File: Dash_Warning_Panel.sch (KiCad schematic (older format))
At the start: 39 parts, among them J1 Conn, U1 TLC6C5816, U2 TPS22810

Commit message: 2020 Initial Design
2020 Initial Design Submission:
Connector changed to 8 pin Molex 90 degree KK
Added Seven Segment Display
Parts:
- removed HS1: Heatsink_Pad, symbol Mechanical:Heatsink_Pad
- C1, C2, C3, C4, C5, C6, C7: Digikey P/N (none) -> 399-11133-1-ND
- C8: Digikey P/N (none) -> 399-1096-1-ND; P/N (none) -> C0603C104K4RACTU
- D2, D3, D4, D5, D6: footprint LEDs:LED_Cree-PLCC4_2x2mm_CW -> OSRAM:OSRAM_PLCC-4_THERM_PAD
- J1: footprint Connectors_TE-Connectivity:TE_84953-6_1x06_P1.0mm_Horizontal -> Molex:Molex_KK-171857_08x2.54mm_Right_Angle; Digikey P/N A101400CT-ND -> WM10303-ND; MFG TE -> Molex; P/N ‎84953-6 -> 1718571008
- R1: value 11.3 -> 11; footprint Resistors_SMD:R_0603 -> Resistors_SMD:R_1210; Digikey P/N 541-27.4HCT-ND -> 541-11.0AACT-ND; P/N CRCW060327R4FKEA -> CRCW121011R0FKEA
- R10: value 86.6 -> 118; Digikey P/N (none) -> 541-118HCT-ND; MFG (none) -> Vishay; P/N ‎1-2176091-8 -> CRCW0603118RFKEA
- R11, R12, R13, R14, R15, R16, R17, R7, R8, R9: value 116.7 -> 118; Digikey P/N 541-27.4HCT-ND -> 541-118HCT-ND; P/N CRCW060327R4FKEA -> CRCW0603118RFKEA
- R2, R3, R4, R5, R6: value 71 -> 69.8; footprint Resistors_SMD:R_0603 -> Resistors_SMD:R_1206; Digikey P/N 541-27.4HCT-ND -> 541-69.8FCT-ND; P/N CRCW060327R4FKEA -> CRCW120669R8FKEA
- U1: Digikey P/N (none) -> 296-51674-1-ND; MFG (none) -> TI; P/N (none) -> TLC6C5816QPWPRQ1
- U2: Digikey P/N (none) -> 296-45297-1-ND
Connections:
- net labels removed: HS
- wire segments 151 -> 152
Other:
- note added: "*Pad 26 Net reused as heatsink \npad net for flood fill clearancing"
- note added: "Blue: LCB G6SP\nIfm = 250mA, Ifn = 150mA\nVf = 3.3V, Vin = 5.0V\nVr = 5-3.3= 1.70V\nR = 1.70V/150mA = 11.3 Ohm\nVrm = 2.1V, Irm = 200mA\nVrmin = 10.5 Ohm\nPr = 2.1 * 200mA = 0.42W"
- note added: "Green: KP DELPS\nIfm = 20mA, Ifn = 18mA\nVf = 2.9V, Vin = 5.0V\nVr = 5-2.9= 2.10V\nR = 2.10V/18mA = 116.7 Ohm\nVrm = 2.3V, Irm = 20mA\nVrmin = 115 Ohm\nPr = 2.3 * 20mA = 0.046W"
- note added: "Red: LS E6SF\nIfm = 70mA, Ifn = 40mA\nVf = 2.15V, Vin = 5.0V\nVr = 5.0-2.15 = 2.85V\nR = 2.85V/40mA = 71.25 Ohm\nVrm = 3.0V, Irm = 50mA\nVrmin = 60 Ohm\nPr = 3V * 50mA = 0.15W"
- note added: "Seg: DSM7TA56105T\nIfm = 20mA, Ifn = 18mA\nVf = 3.0V, Vin = 5.0V\nVr = 5-3.0= 2.00V\nR = 2.00V/18mA = 111.1 Ohm\nVrm = 2.2V, Irm = 20mA\nVrmin = 110 Ohm\nPr = 2.2V * 20mA = 0.044W"
- note added: "Yellow: LY E6SF\nIfm = 70mA, Ifn = 40mA\nVf = 2.15V, Vin = 5.0V\nVr = 5.0-2.15 = 2.85V\nR = 2.85V/40mA = 71.25 Ohm\nVrm = 3.0V, Irm = 50mA\nVrmin = 60 Ohm\nPr = 3V * 50mA = 0.15W"
- note removed: "Blue: LCB G6SP\nIfm = 250mA, Ifn = 150mA\nVf = 3.3V, Vin = 5.0V\nVr = 5-3.3= 1.70V\nR = 1.70V/150mA = 11.3 Ohm\nVrm = 2.1V, Irm = 200mA\nVrmin = 10.5 Ohm"
- note removed: "Green: KP DELPS\nIfm = 20mA, Ifn = 18mA\nVf = 2.9V, Vin = 5.0V\nVr = 5-2.9= 2.10V\nR = 2.10V/18mA = 116.7 Ohm\nVrm = 2.3V, Irm = 20mA\nVrmin = 115 Ohm"
- note removed: "Red: LS E6SF\nIfm = 70mA, Ifn = 40mA\nVf = 2.15V, Vin = 5.0V\nVr = 5.0-2.15 = 2.85V\nR = 2.85V/40mA = 71.25 Ohm\nVrm = 3.0V, Irm = 50mA\nVrmin = 60 Ohm"
- note removed: "Seg: DSM7TA56105T\nIfm = 20mA, Ifn = 18mA\nVf = 3.0V, Vin = 5.0V\nVr = 5-3.0= 2.00V\nR = 2.00V/18mA = 111.1 Ohm\nVrm = 2.2V, Irm = 20mA\nVrmin = 110 Ohm"
- note removed: "Yellow: LY E6SF\nIfm = 70mA, Ifn = 40mA\nVf = 2.15V, Vin = 5.0V\nVr = 5.0-2.15 = 2.85V\nR = 2.85V/40mA = 71.25 Ohm\nVrm = 3.0V, Irm = 50mA\nVrmin = 60 Ohm"

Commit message: First Manufacture Ready 2020
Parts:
- C1, C2, C3, C4, C5, C6, C7: Digikey P/N 399-11133-1-ND -> (none); MFG KEMET -> (none); P/N C0603C105K8RACTU -> (none)
- C8: Description (none) -> CAP CER 0.1UF 16V X7R 0603; Digikey P/N 399-1096-1-ND -> (none); P/N C0603C104K4RACTU -> C0603C104M4RACTU
- D2, D6: value LY E6SF -> SM1206NYC-IL; footprint OSRAM:OSRAM_PLCC-4_THERM_PAD -> LEDs:LED_1206; Description (none) -> LED YELLOW CLEAR 1206 SMD; Digikey P/N 475-3790-1-ND -> (none); MFG OSRAM -> BIVAR; P/N LY E6SF-ABCA-36-3B5A-50-R18-Z -> SM1206NYC-IL
- D3, D4, D5: value LS E6SF -> SM1206NHC-IL; footprint OSRAM:OSRAM_PLCC-4_THERM_PAD -> LEDs:LED_1206; Description (none) -> LED RED CLEAR 1206 SMD; Digikey P/N 475-3432-1-ND -> (none); MFG OSRAM -> BIVAR; P/N LS E67F-ABBB-1-1-Z -> SM1206NHC-IL
- D7, D8, D9: value KP DELPS -> SM1206NPGC-IL; footprint OSRAM:PLCC-2 -> LEDs:LED_1206; Description (none) -> LED GREEN CLEAR 1206 SMD; Digikey P/N 475-3715-1-ND -> (none); MFG OSRAM -> BIVAR; P/N KP DELPS1.FP-UGVI-34-Z555-10-S -> SM1206NPGC-IL
- J1: footprint Molex:Molex_KK-171857_08x2.54mm_Right_Angle -> FSAE-Dash-Warning-Panel:8wireConn; Digikey P/N WM10303-ND -> N/A; MFG Molex -> N/A; P/N 1718571008 -> N/A
- R1: Digikey P/N 541-11.0AACT-ND -> (none)
- R10, R11, R12, R13, R14, R15, R16, R17, R7, R8, R9: value 118 -> 120; Description (none) -> RES 120 OHM 1% 1/10W 0603; Digikey P/N 541-118HCT-ND -> RMCF0603FT120RCT-ND; MFG Vishay -> Stackpole; P/N CRCW0603118RFKEA -> RMCF0603FT120R
- R2, R3, R4, R5, R6: value 69.8 -> 120; footprint Resistors_SMD:R_1206 -> Resistors_SMD:R_0603; Description (none) -> RES 120 OHM 1% 1/10W 0603; Digikey P/N 541-69.8FCT-ND -> RMCF0603FT120RCT-ND; MFG Vishay -> Stackpole; P/N CRCW120669R8FKEA -> RMCF0603FT120R
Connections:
- net GND: now also U1.29 (HS)
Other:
- note added: "Green - SM1206NPGC-IL\nVf = 3V, 1550mcd @ 523nm\nIf = 20mA, Ifp = 100mA\nMin R: 100 Ohm\nPr = 2.0 * 20mA = 0.040W"
- note added: "Red SM1206NHC-IL\nVf = 2.1V, 1250mcd @ 630nm\nIf = 25mA, Ifp = 100mA\nVin = 5.0V\nVr = 5.0-2.10 = 2.90V\nR = 2.90V/25mA = 116 Ohm\nPr = 2.9V * 25mA = 0.0725W"
- note added: "Yellow - SM1206NYC-IL\nVf = 2.0V, 1000mcd @ 590nm\nIf = 25mA, Ifp = 100mA\nMin R: 120 Ohm\nPr = 3V * 25mA = 0.075W"
- note removed: "*Pad 26 Net reused as heatsink \npad net for flood fill clearancing"
- note removed: "Green: KP DELPS\nIfm = 20mA, Ifn = 18mA\nVf = 2.9V, Vin = 5.0V\nVr = 5-2.9= 2.10V\nR = 2.10V/18mA = 116.7 Ohm\nVrm = 2.3V, Irm = 20mA\nVrmin = 115 Ohm\nPr = 2.3 * 20mA = 0.046W"
- note removed: "Red: LS E6SF\nIfm = 70mA, Ifn = 40mA\nVf = 2.15V, Vin = 5.0V\nVr = 5.0-2.15 = 2.85V\nR = 2.85V/40mA = 71.25 Ohm\nVrm = 3.0V, Irm = 50mA\nVrmin = 60 Ohm\nPr = 3V * 50mA = 0.15W"
- note removed: "Yellow: LY E6SF\nIfm = 70mA, Ifn = 40mA\nVf = 2.15V, Vin = 5.0V\nVr = 5.0-2.15 = 2.85V\nR = 2.85V/40mA = 71.25 Ohm\nVrm = 3.0V, Irm = 50mA\nVrmin = 60 Ohm\nPr = 3V * 50mA = 0.15W"

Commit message: Updated BOM and part number data
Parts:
- C1, C2, C3, C4, C5, C6, C7: Description (none) -> CAP CER 1.0UF 16V X7R 0603; Digikey P/N (none) -> 399-7847-1-ND; MFG (none) -> KEMET; P/N (none) -> C0603C105K4RACTU
- C8: Digikey P/N (none) -> 399-1099-1-ND
- D1: Description (none) -> LED BLUE, 3.3V 140mA
- D10: Description (none) -> DISPLAY 7SEG 0.56\" SGL GRN 10SMD
- D2, D6: Digikey P/N (none) -> 492-1947-1-ND
- D3, D4, D5: Digikey P/N (none) -> 492-1944-1-ND
- D7, D8, D9: Digikey P/N (none) -> 492-1945-1-ND
- J1: Description (none) -> Wire Solder Points
- R1: Description (none) -> RES SMD 11 OHM 1% 1/2W 1210; Digikey P/N (none) -> 541-11.0AACT-ND
- U1: Description (none) -> LED Driver IC 16 Output Linear Shift Register PWM Dimming
- U2: Description (none) -> IC PWR SWITCH N-CHAN 1:1 SOT23-6
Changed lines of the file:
@@
 F 2 "Capacitors_SMD:C_0603" H 5038 1000 50  0001 C CNN
 F 3 "" H 5000 1150 50  0001 C CNN
-F 4 "" H 0   0   50  0001 C CNN "P/N"
-F 5 "" H 5000 1150 50  0001 C CNN "MFG"
-F 6 "" H 5000 1150 50  0001 C CNN "Digikey P/N"
+F 4 "C0603C105K4RACTU" H 0   0   50  0001 C CNN "P/N"
+F 5 "KEMET" H 5000 1150 50  0001 C CNN "MFG"
+F 6 "399-7847-1-ND" H 5000 1150 50  0001 C CNN "Digikey P/N"
+F 7 "CAP CER 1.0UF 16V X7R 0603" H 5000 1150 50  0001 C CNN "Description"
 	1    5000 1150
 	1    0    0    -1
@@
 F 2 "Capacitors_SMD:C_0603" H 5338 1000 50  0001 C CNN
 F 3 "" H 5300 1150 50  0001 C CNN
-F 4 "" H 0   0   50  0001 C CNN "P/N"
-F 5 "" H 5300 1150 50  0001 C CNN "MFG"
-F 6 "" H 5300 1150 50  0001 C CNN "Digikey P/N"
+F 4 "C0603C105K4RACTU" H 0   0   50  0001 C CNN "P/N"
+F 5 "KEMET" H 5300 1150 50  0001 C CNN "MFG"
+F 6 "399-7847-1-ND" H 5300 1150 50  0001 C CNN "Digikey P/N"
+F 7 "CAP CER 1.0UF 16V X7R 0603" H 5300 1150 50  0001 C CNN "Description"
 	1    5300 1150
 	1    0    0    -1
@@
 F 2 "Capacitors_SMD:C_0603" H 5638 1000 50  0001 C CNN
 F 3 "" H 5600 1150 50  0001 C CNN
-F 4 "" H 0   0   50  0001 C CNN "P/N"
-F 5 "" H 5600 1150 50  0001 C CNN "MFG"
-F 6 "" H 5600 1150 50  0001 C CNN "Digikey P/N"
+F 4 "C0603C105K4RACTU" H 0   0   50  0001 C CNN "P/N"
+F 5 "KEMET" H 5600 1150 50  0001 C CNN "MFG"
+F 6 "399-7847-1-ND" H 5600 1150 50  0001 C CNN "Digikey P/N"
+F 7 "CAP CER 1.0UF 16V X7R 0603" H 5600 1150 50  0001 C CNN "Description"
 	1    5600 1150
 	1    0    0    -1
@@
 F 5 "N/A" H 1950 3600 50  0001 C CNN "Digikey P/N"
 F 6 "N/A" H 1950 3600 50  0001 C CNN "MFG"
+F 7 "Wire Solder Points" H 1950 3600 50  0001 C CNN "Description"
 	1    1950 3600
 	-1   0    0    -1
@@
 F 3 "https://www.bivar.com/Files/Datasheets/SM1206NYC-IL.pdf" H 7650 4600 50  0001 C CNN
 F 4 "SM1206NYC-IL" H 300 -1000 50  0001 C CNN "P/N"
-F 5 "" H 7650 4600 50  0001 C CNN "Digikey P/N"
+F 5 "492-1947-1-ND" H 7650 4600 50  0001 C CNN "Digikey P/N"
 F 6 "BIVAR" H 7650 4600 50  0001 C CNN "MFG"
 F 7 "LED YELLOW CLEAR 1206 SMD" H 7650 4600 50  0001 C CNN "Description"
@@
 F 5 "TI" H 3550 1150 50  0001 C CNN "MFG"
 F 6 "296-45297-1-ND" H 3550 1150 50  0001 C CNN "Digikey P/N"
+F 7 "IC PWR SWITCH N-CHAN 1:1 SOT23-6" H 3550 1150 50  0001 C CNN "Description"
 	1    3550 1150
 	1    0    0    -1
@@
 F 2 "Capacitors_SMD:C_0603" H 2838 1450 50  0001 C CNN
 F 3 "" H 2800 1600 50  0001 C CNN
-F 4 "" H 0   0   50  0001 C CNN "P/N"
-F 5 "" H 2800 1600 50  0001 C CNN "MFG"
-F 6 "" H 2800 1600 50  0001 C CNN "Digikey P/N"
+F 4 "C0603C105K4RACTU" H 0   0   50  0001 C CNN "P/N"
+F 5 "KEMET" H 2800 1600 50  0001 C CNN "MFG"
+F 6 "399-7847-1-ND" H 2800 1600 50  0001 C CNN "Digikey P/N"
+F 7 "CAP CER 1.0UF 16V X7R 0603" H 2800 1600 50  0001 C CNN "Description"
 	1    2800 1600
 	-1   0    0    1
@@
 F 2 "Capacitors_SMD:C_0603" H 4388 1450 50  0001 C CNN
 F 3 "" H 4350 1600 50  0001 C CNN
-F 4 "" H 0   0   50  0001 C CNN "P/N"
-F 5 "" H 4350 1600 50  0001 C CNN "MFG"
-F 6 "" H 4350 1600 50  0001 C CNN "Digikey P/N"
+F 4 "C0603C105K4RACTU" H 0   0   50  0001 C CNN "P/N"
+F 5 "KEMET" H 4350 1600 50  0001 C CNN "MFG"
+F 6 "399-7847-1-ND" H 4350 1600 50  0001 C CNN "Digikey P/N"
+F 7 "CAP CER 1.0UF 16V X7R 0603" H 4350 1600 50  0001 C CNN "Description"
 	1    4350 1600
 	-1   0    0    1
@@
 F 2 "Capacitors_SMD:C_0603" H 2588 3050 50  0001 C CNN
 F 3 "" H 2550 3200 50  0001 C CNN
-F 4 "" H 0   0   50  0001 C CNN "P/N"
-F 5 "" H 2550 3200 50  0001 C CNN "MFG"
-F 6 "" H 2550 3200 50  0001 C CNN "Digikey P/N"
+F 4 "C0603C105K4RACTU" H 0   0   50  0001 C CNN "P/N"
+F 5 "KEMET" H 2550 3200 50  0001 C CNN "MFG"
+F 6 "399-7847-1-ND" H 2550 3200 50  0001 C CNN "Digikey P/N"
+F 7 "CAP CER 1.0UF 16V X7R 0603" H 2550 3200 50  0001 C CNN "Description"
 	1    2550 3200
 	1    0    0    -1
@@
 F 1 "LCB G6SP" H 6450 1450 50  0000 C CNN
 F 2 "OSRAM:PLCC-6_THERM_MOD" H 6450 1350 50  0001 C CNN
-F 3 "" H 6450 1350 50  0001 C CNN
+F 3 "https://dammedia.osram.info/media/resource/hires/osram-dam-6030625/LCB%20G6SP_EN.pdf" H 6450 1350 50  0001 C CNN
 F 4 "LCB G6SP-DBFA-4J5L-0-140-R18-Z" H -900 -4250 50  0001 C CNN "P/N"
 F 5 "475-3674-1-ND" H 6450 1350 50  0001 C CNN "Digikey P/N"
 F 6 "OSRAM" H 6450 1350 50  0001 C CNN "MFG"
+F 7 "LED BLUE, 3.3V 140mA" H 6450 1350 50  0001 C CNN "Description"
 	1    6450 1350
 	0    -1   -1   0
@@
 F 3 "https://www.bivar.com/Portals/0/Products/SM1206NHC-IL.pdf" H 7650 4250 50  0001 C CNN
 F 4 "SM1206NHC-IL" H 300 -1350 50  0001 C CNN "P/N"
-F 5 "" H 7650 4250 50  0001 C CNN "Digikey P/N"
+F 5 "492-1944-1-ND" H 7650 4250 50  0001 C CNN "Digikey P/N"
 F 6 "BIVAR" H 7650 4250 50  0001 C CNN "MFG"
 F 7 "LED RED CLEAR 1206 SMD" H 7650 4250 50  0001 C CNN "Description"
@@
 F 1 "11" V 6450 1750 50  0000 C CNN
 F 2 "Resistors_SMD:R_1210" V 6380 1750 50  0001 C CNN
-F 3 "" H 6450 1750 50  0001 C CNN
+F 3 "http://www.vishay.com/docs/20035/dcrcwe3.pdf" H 6450 1750 50  0001 C CNN
 F 4 "CRCW121011R0FKEA" H -450 -3850 50  0001 C CNN "P/N"
-F 5 "" H 6450 1750 50  0001 C CNN "Digikey P/N"
+F 5 "541-11.0AACT-ND" H 6450 1750 50  0001 C CNN "Digikey P/N"
 F 6 "Vishay" H 6450 1750 50  0001 C CNN "MFG"
+F 7 "RES SMD 11 OHM 1% 1/2W 1210" H 6450 1750 50  0001 C CNN "Description"
 	1    6450 1750
 	1    0    0    -1
@@
 F 3 "https://www.bivar.com/Portals/0/Products/SM1206NHC-IL.pdf" H 7650 3900 50  0001 C CNN
 F 4 "SM1206NHC-IL" H 300 -1700 50  0001 C CNN "P/N"
-F 5 "" H 7650 3900 50  0001 C CNN "Digikey P/N"
+F 5 "492-1944-1-ND" H 7650 3900 50  0001 C CNN "Digikey P/N"
 F 6 "BIVAR" H 7650 3900 50  0001 C CNN "MFG"
 F 7 "LED RED CLEAR 1206 SMD" H 7650 3900 50  0001 C CNN "Description"
@@
 F 3 "https://www.bivar.com/Portals/0/Products/SM1206NHC-IL.pdf" H 7650 3550 50  0001 C CNN
 F 4 "SM1206NHC-IL" H 300 -2050 50  0001 C CNN "P/N"
-F 5 "" H 7650 3550 50  0001 C CNN "Digikey P/N"
+F 5 "492-1944-1-ND" H 7650 3550 50  0001 C CNN "Digikey P/N"
 F 6 "BIVAR" H 7650 3550 50  0001 C CNN "MFG"
 F 7 "LED RED CLEAR 1206 SMD" H 7650 3550 50  0001 C CNN "Description"
@@
 F 3 "https://www.bivar.com/Files/Datasheets/SM1206NYC-IL.pdf" H 7650 3200 50  0001 C CNN
 F 4 "SM1206NYC-IL" H 300 -2400 50  0001 C CNN "P/N"
-F 5 "" H 7650 3200 50  0001 C CNN "Digikey P/N"
+F 5 "492-1947-1-ND" H 7650 3200 50  0001 C CNN "Digikey P/N"
 F 6 "BIVAR" H 7650 3200 50  0001 C CNN "MFG"
 F 7 "LED YELLOW CLEAR 1206 SMD" H 7650 3200 50  0001 C CNN "Description"
@@
 F 3 "https://www.bivar.com/parts_content/Datasheets/SM1206NPGC-IL.pdf" H 7650 2850 50  0001 C CNN
 F 4 "SM1206NPGC-IL" H 300 -2750 50  0001 C CNN "P/N"
-F 5 "" H 7650 2850 50  0001 C CNN "Digikey P/N"
+F 5 "492-1945-1-ND" H 7650 2850 50  0001 C CNN "Digikey P/N"
 F 6 "BIVAR" H 7650 2850 50  0001 C CNN "MFG"
 F 7 "LED GREEN CLEAR 1206 SMD" H 7650 2850 50  0001 C CNN "Description"
@@
 F 3 "https://www.bivar.com/parts_content/Datasheets/SM1206NPGC-IL.pdf" H 7650 2500 50  0001 C CNN
 F 4 "SM1206NPGC-IL" H 300 -3100 50  0001 C CNN "P/N"
-F 5 "" H 7650 2500 50  0001 C CNN "Digikey P/N"
+F 5 "492-1945-1-ND" H 7650 2500 50  0001 C CNN "Digikey P/N"
 F 6 "BIVAR" H 7650 2500 50  0001 C CNN "MFG"
 F 7 "LED GREEN CLEAR 1206 SMD" H 7650 2500 50  0001 C CNN "Description"
@@
 F 3 "https://www.bivar.com/parts_content/Datasheets/SM1206NPGC-IL.pdf" H 7650 2150 50  0001 C CNN
 F 4 "SM1206NPGC-IL" H 300 -3450 50  0001 C CNN "P/N"
-F 5 "" H 7650 2150 50  0001 C CNN "Digikey P/N"
+F 5 "492-1945-1-ND" H 7650 2150 50  0001 C CNN "Digikey P/N"
 F 6 "BIVAR" H 7650 2150 50  0001 C CNN "MFG"
 F 7 "LED GREEN CLEAR 1206 SMD" H 7650 2150 50  0001 C CNN "Description"
@@
 F 5 "DSM7TA56105TCT-ND" H 7050 5850 50  0001 C CNN "Digikey P/N"
 F 6 "DSM7TA56105T" H 7050 5850 50  0001 C CNN "P/N"
+F 7 "DISPLAY 7SEG 0.56\" SGL GRN 10SMD" H 7050 5850 50  0001 C CNN "Description"
 	1    7050 5850
 	1    0    0    -1
@@
 F 5 "TI" H 5550 3350 50  0001 C CNN "MFG"
 F 6 "TLC6C5816QPWPRQ1" H 5550 3350 50  0001 C CNN "P/N"
+F 7 "LED Driver IC 16 Output Linear Shift Register PWM Dimming" H 5550 3350 50  0001 C CNN "Description"
 	1    5550 3350
 	1    0    0    -1
@@
 F 2 "Capacitors_SMD:C_0603" H 4138 2650 50  0001 C CNN
 F 3 "" H 4100 2800 50  0001 C CNN
-F 4 "" H 1550 -400 50  0001 C CNN "P/N"
-F 5 "" H 4100 2800 50  0001 C CNN "MFG"
-F 6 "" H 4100 2800 50  0001 C CNN "Digikey P/N"
+F 4 "C0603C105K4RACTU" H 1550 -400 50  0001 C CNN "P/N"
+F 5 "KEMET" H 4100 2800 50  0001 C CNN "MFG"
+F 6 "399-7847-1-ND" H 4100 2800 50  0001 C CNN "Digikey P/N"
+F 7 "CAP CER 1.0UF 16V X7R 0603" H 4100 2800 50  0001 C CNN "Description"
 	1    4100 2800
 	1    0    0    -1
@@
 F 4 "C0603C104M4RACTU" H 1850 -400 50  0001 C CNN "P/N"
 F 5 "KEMET" H 4400 2800 50  0001 C CNN "MFG"
-F 6 "" H 4400 2800 50  0001 C CNN "Digikey P/N"
+F 6 "399-1099-1-ND" H 4400 2800 50  0001 C CNN "Digikey P/N"
 F 7 "CAP CER 0.1UF 16V X7R 0603" H 4400 2800 50  0001 C CNN "Description"
 	1    4400 2800
@@
 	2950 3400 2550 3400
 Connection ~ 2550 3400
+$Comp
+L power:GND #PWR?
+U 1 1 5EF8AEF3
+P 5450 4250
+F 0 "#PWR?" H 5450 4000 50  0001 C CNN
+F 1 "GND" H 5455 4077 50  0000 C CNN
+F 2 "" H 5450 4250 50  0001 C CNN
+F 3 "" H 5450 4250 50  0001 C CNN
+	1    5450 4250
+	1    0    0    -1
+$EndComp
 Wire Bus Line
 	4700 4850 6750 4850
@@
 Wire Bus Line
 	4700 3050 4700 4850
-$Comp
-L power:GND #PWR?
-U 1 1 5EF8AEF3
-P 5450 4250
-F 0 "#PWR?" H 5450 4000 50  0001 C CNN
-F 1 "GND" H 5455 4077 50  0000 C CNN
-F 2 "" H 5450 4250 50  0001 C CNN
-F 3 "" H 5450 4250 50  0001 C CNN
-	1    5450 4250
-	1    0    0    -1
-$EndComp
 $EndSCHEMATC

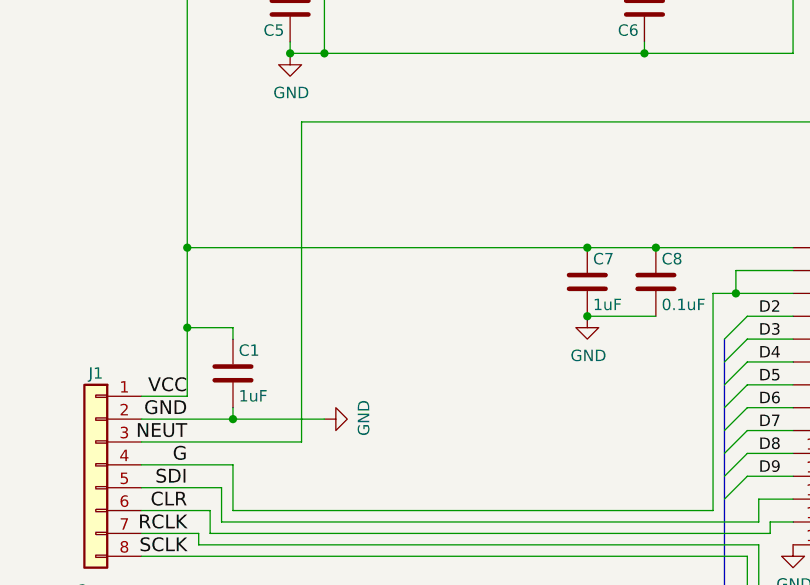
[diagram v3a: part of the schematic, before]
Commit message: Added LDO 3.3V Reg
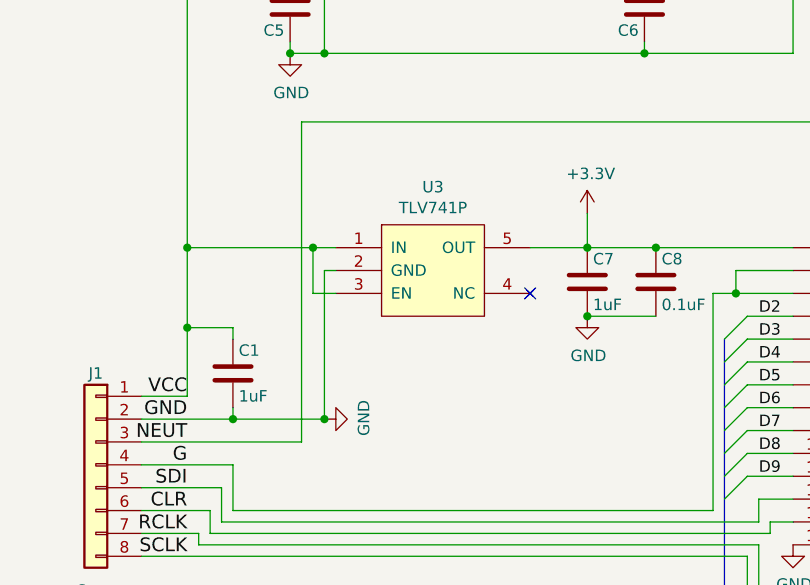
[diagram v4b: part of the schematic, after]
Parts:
- added U3: TLV741P, TO_SOT_Packages_SMD:SOT-23-5, symbol TI-addition:TLV741P
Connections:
- net GND: now also U3.2 (GND)
- net VCC: now also U3.1 (IN), U3.3 (EN); no longer C7.1, C8.1, U1.1 (VCC)
- new net +3V3: C7.1, C8.1, U1.1 (VCC), U3.5 (OUT)
- no-connect marks 5 -> 6
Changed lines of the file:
@@
 Wire Wire Line
 	2350 3300 2150 3300
-Wire Wire Line
-	2350 1000 2350 2650
 $Comp
 L Device:LED_ALT D2
@@
 Wire Wire Line
 	2150 4000 4800 4000
-Wire Wire Line
-	4100 2650 2350 2650
-Connection ~ 4100 2650
-Connection ~ 2350 2650
-Wire Wire Line
-	2350 2650 2350 3000
 Text Label 2350 3800 2    60   ~ 0
 CLR
@@
 Connection ~ 2550 3400
 $Comp
-L power:GND #PWR?
+L power:GND #PWR0106
 U 1 1 5EF8AEF3
 P 5450 4250
-F 0 "#PWR?" H 5450 4000 50  0001 C CNN
+F 0 "#PWR0106" H 5450 4000 50  0001 C CNN
 F 1 "GND" H 5455 4077 50  0000 C CNN
 F 2 "" H 5450 4250 50  0001 C CNN
@@
 	1    0    0    -1
 $EndComp
+Wire Wire Line
+	2350 1000 2350 2650
+$Comp
+L TI-addition:TLV741P U3
+U 1 1 5F3CBD45
+P 3400 2750
+F 0 "U3" H 3425 3115 50  0000 C CNN
+F 1 "TLV741P" H 3425 3024 50  0000 C CNN
+F 2 "TO_SOT_Packages_SMD:SOT-23-5" H 3400 2400 50  0001 C CNN
+F 3 "https://www.ti.com/lit/ds/symlink/tlv741p.pdf" H 3000 2850 50  0001 C CNN
+F 4 "IC REG LINEAR 3.3V 150MA SOT23-5" H 3400 2750 50  0001 C CNN "Description"
+F 5 "296-48987-1-ND" H 3400 2750 50  0001 C CNN "Digikey P/N"
+F 6 "TI" H 3400 2750 50  0001 C CNN "MFG"
+F 7 "TLV74133PDBVR" H 3400 2750 50  0001 C CNN "P/N"
+	1    3400 2750
+	1    0    0    -1
+$EndComp
+NoConn ~ 3850 2850
+Wire Wire Line
+	3850 2650 4100 2650
+Connection ~ 4100 2650
+Wire Wire Line
+	3000 2650 2900 2650
+Connection ~ 2350 2650
+Wire Wire Line
+	2350 2650 2350 3000
+Wire Wire Line
+	3000 2850 2900 2850
+Wire Wire Line
+	2900 2850 2900 2650
+Connection ~ 2900 2650
+Wire Wire Line
+	2900 2650 2350 2650
+Wire Wire Line
+	3000 2750 2950 2750
+Wire Wire Line
+	2950 2750 2950 3400
+Connection ~ 2950 3400
+$Comp
+L power:+3.3V #PWR0107
+U 1 1 5F3F700F
+P 4100 2500
+F 0 "#PWR0107" H 4100 2350 50  0001 C CNN
+F 1 "+3.3V" H 4115 2673 50  0000 C CNN
+F 2 "" H 4100 2500 50  0001 C CNN
+F 3 "" H 4100 2500 50  0001 C CNN
+	1    4100 2500
+	1    0    0    -1
+$EndComp
+Wire Wire Line
+	4100 2500 4100 2650
 Wire Bus Line
 	4700 4850 6750 4850

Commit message: Release Candidate 1
Fixed Blue LED ambiguity
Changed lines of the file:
@@
 Text Label 7350 2150 0    50   ~ 0
 D9_h
-Entry Wire Line
-	6750 2400 6850 2500
-Entry Wire Line
-	6750 2750 6850 2850
 Wire Wire Line
 	7800 4600 8000 4600
@@
 Wire Wire Line
 	8000 4250 8000 3900
-Entry Wire Line
-	6750 3100 6850 3200
-Entry Wire Line
-	6750 3450 6850 3550
-Entry Wire Line
-	6750 3800 6850 3900
-Entry Wire Line
-	6750 4150 6850 4250
-Entry Wire Line
-	6750 4500 6850 4600
 Wire Wire Line
 	6850 4600 7050 4600
@@
 	7050 2150 6850 2150
 Entry Wire Line
-	6750 2050 6850 2150
+	6750 2250 6850 2150
 Entry Bus Bus
 	5700 4850 5800 4950
@@
 Wire Wire Line
 	4100 2500 4100 2650
+Entry Wire Line
+	6750 2600 6850 2500
+Entry Wire Line
+	6750 2950 6850 2850
+Entry Wire Line
+	6750 3300 6850 3200
+Entry Wire Line
+	6750 3650 6850 3550
+Entry Wire Line
+	6750 4000 6850 3900
+Entry Wire Line
+	6750 4350 6850 4250
+Entry Wire Line
+	6750 4700 6850 4600
 Wire Bus Line
 	4700 4850 6750 4850
@@
 	6400 3150 6400 4750
 Wire Bus Line
-	6750 2050 6750 4850
+	6750 2250 6750 4850
 Wire Bus Line
 	4700 3050 4700 4850
